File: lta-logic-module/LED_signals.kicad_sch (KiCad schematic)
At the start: 12 parts

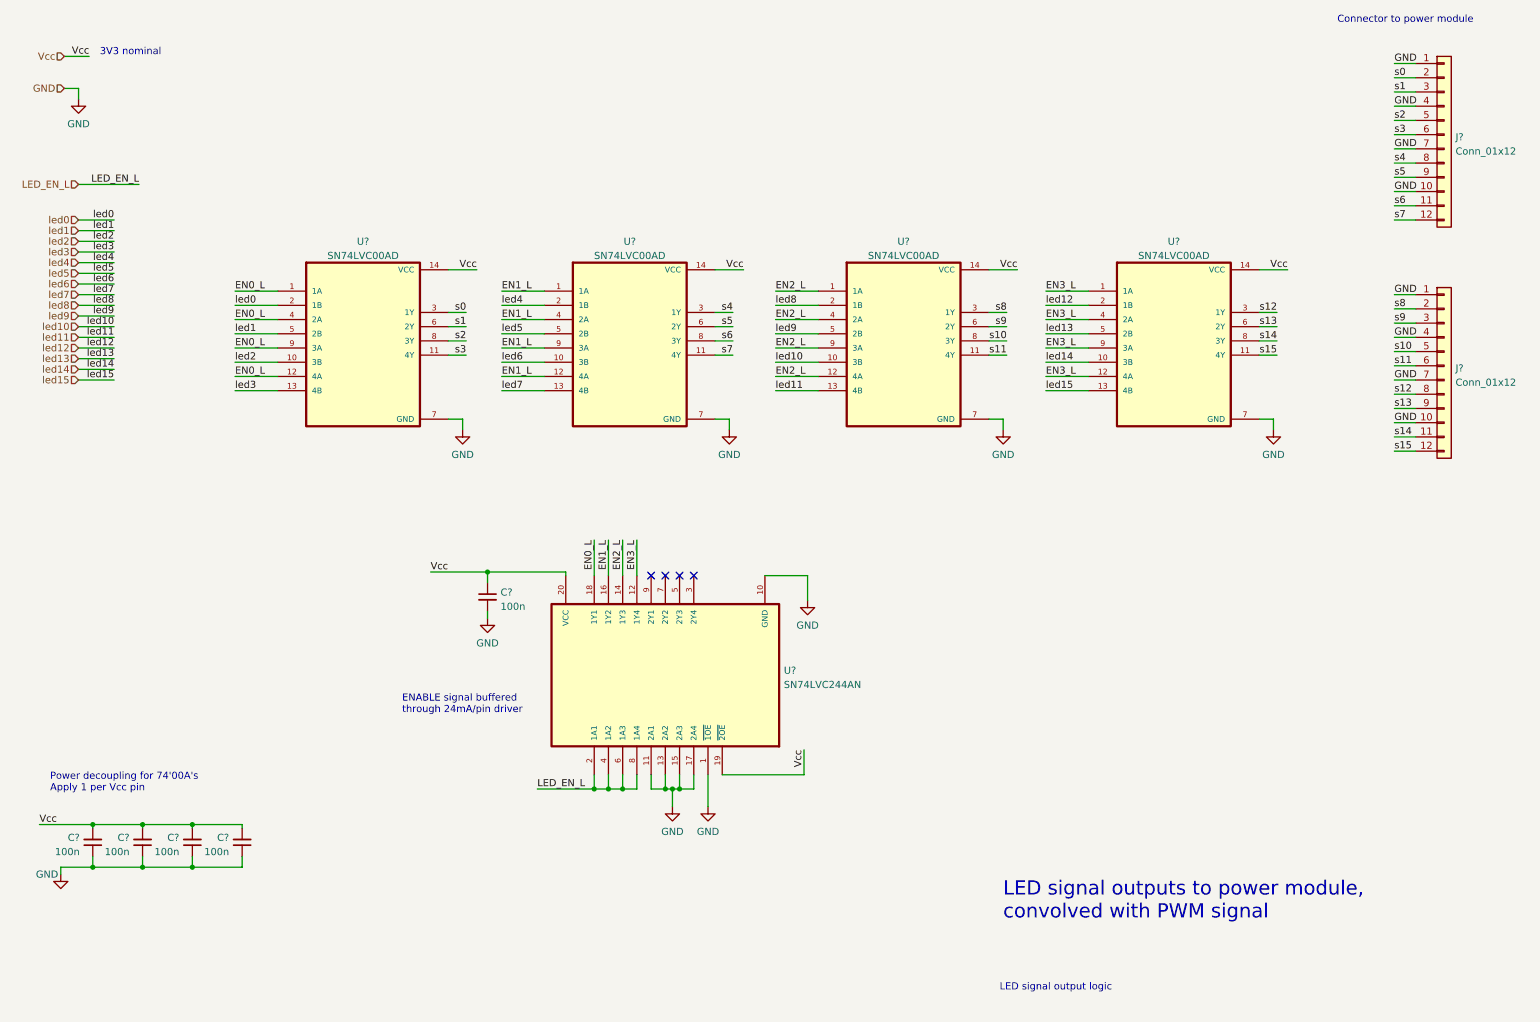
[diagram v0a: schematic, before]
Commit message: Fix ERC violations.
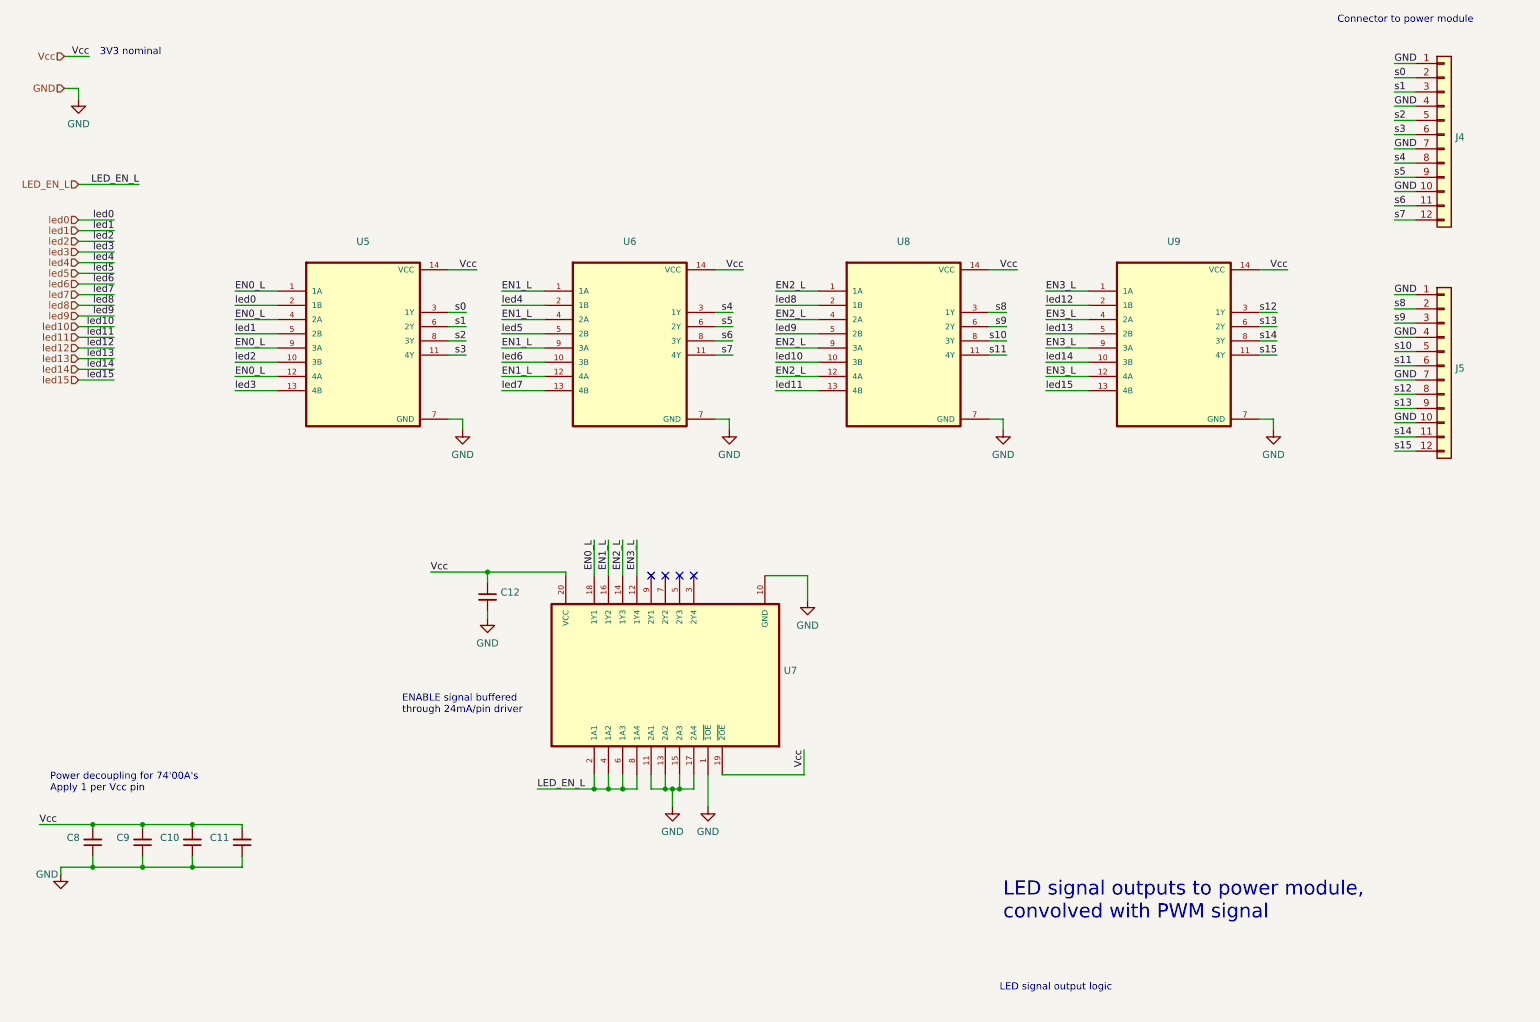
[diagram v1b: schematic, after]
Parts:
- C10, C11, C12, C8, C9: renamed from C?; value 100n -> (none)
- J4, J5: renamed from J?; value Conn_01x12 -> (none)
- U5, U6, U8, U9: renamed from U?; value SN74LVC00AD -> (none); footprint Aaron_TI_Parts:TI_SOIC_D_R-PDSO-G14 -> (none)
- U7: renamed from U?; value SN74LVC244AN -> (none); footprint Aaron_TI_Parts:TI_N_R-PDIP-T20 -> (none)

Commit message: Add TODOs, update some footprints.
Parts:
- C10, C11, C12, C8, C9: value (none) -> 100n; footprint (none) -> Capacitor_SMD:C_0603_1608Metric; Comment (none) -> 100nF 5% 6.3V 0603 X7R ceramic; 20mOhm < ESR < 10 Ohm; MANUFACTURER (none) -> KYOCERA; MPN (none) -> 06036C104JAT2A
- J4, J5: value (none) -> Conn_01x12; footprint (none) -> Connector_PinHeader_2.54mm:PinHeader_1x12_P2.54mm_Vertical; Comment (none) -> TODO REPLACE FOOTPRINT; MPN (none) -> XXX TODO FIND
- U5, U6, U8, U9: value (none) -> SN74LVC00AD; footprint (none) -> Aaron_TI_Parts:TI_SOIC_D_R-PDSO-G14; MANUFACTURER (none) -> Texas Instruments; MPN (none) -> SN74LVC00AD
- U7: value (none) -> SN74LVC244AN; footprint (none) -> Aaron_TI_Parts:TI_N_R-PDIP-T20; MANUFACTURER (none) -> Texas Instruments; MPN (none) -> SN74LVC244AN

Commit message: Initial PCB setup
* Configure Elecrow DRC checks for lta-logic-module.
* Switch SN74LVC244A from 'N' PDIP to 'DWR' SOIC footprint.
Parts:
- removed U7: SN74LVC244AN, Aaron_TI_Parts:TI_N_R-PDIP-T20, symbol Aaron-TI-Buffers:SN74LVC244AN
- added U8: (no value), Aaron_TI_Parts:TI_SOIC_DW0020A, symbol Aaron-TI-Buffers:SN74LVC244ADW
- renumbered C8 to C12, C9 to C13, C10 to C14, C11 to C15, C12 to C16, J4 to J3, J5 to J4, U9 to U10, U5 to U6, U6 to U7, U8 to U9
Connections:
- net EN0_L: now also U8.18 (1Y1)
- net EN1_L: now also U8.16 (1Y2)
- net EN2_L: now also U8.14 (1Y3)
- net EN3_L: now also U8.12 (1Y4)
- net GND: now also U8.1 (~{1OE}), U8.10 (GND), U8.11 (2A1), U8.13 (2A2), U8.15 (2A3), U8.17 (2A4)
- net LED_EN_L: now also U8.2 (1A1), U8.4 (1A2), U8.6 (1A3), U8.8 (1A4)
- net Vcc: now also U8.19 (~{2OE}), U8.20 (VCC)
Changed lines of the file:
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@@
   (symbol (lib_id "Device:C_Small") (at 28.575 163.83 0) (mirror x) (unit 1)
     (in_bom yes) (on_board yes) (fields_autoplaced)
-    (property "Reference" "C8" (id 0) (at 26.2509 162.9889 0)
+    (property "Reference" "C12" (id 0) (at 26.2509 162.9889 0)
       (effects (font (size 1.27 1.27)) (justify right))
     )
@@
   (symbol (lib_id "power:GND") (at 191.135 90.17 0) (unit 1)
     (in_bom yes) (on_board yes) (fields_autoplaced)
-    (property "Reference" "#PWR039" (id 0) (at 191.135 96.52 0)
+    (property "Reference" "#PWR040" (id 0) (at 191.135 96.52 0)
       (effects (font (size 1.27 1.27)) hide)
     )
@@
   (symbol (lib_id "Aaron-TI-74xx:SN74LVC00AD") (at 79.375 78.105 0) (unit 1)
     (in_bom yes) (on_board yes) (fields_autoplaced)
-    (property "Reference" "U5" (id 0) (at 76.835 56.549 0))
+    (property "Reference" "U6" (id 0) (at 76.835 56.549 0))
     (property "Value" "SN74LVC00AD" (id 1) (at 76.835 59.0859 0))
     (property "Footprint" "Aaron_TI_Parts:TI_SOIC_D_R-PDSO-G14" (id 2) (at 74.295 80.645 0)
@@
   (symbol (lib_id "Device:C_Small") (at 55.245 163.83 0) (mirror x) (unit 1)
     (in_bom yes) (on_board yes) (fields_autoplaced)
-    (property "Reference" "C11" (id 0) (at 52.9209 162.9889 0)
+    (property "Reference" "C15" (id 0) (at 52.9209 162.9889 0)
       (effects (font (size 1.27 1.27)) (justify right))
     )
@@
   (symbol (lib_id "Connector_Generic:Conn_01x12") (at 269.875 37.465 0) (unit 1)
     (in_bom yes) (on_board yes) (fields_autoplaced)
-    (property "Reference" "J4" (id 0) (at 271.907 37.9003 0)
+    (property "Reference" "J3" (id 0) (at 271.907 37.9003 0)
       (effects (font (size 1.27 1.27)) (justify left))
     )
@@
   (symbol (lib_id "Aaron-TI-74xx:SN74LVC00AD") (at 224.155 78.105 0) (unit 1)
     (in_bom yes) (on_board yes) (fields_autoplaced)
-    (property "Reference" "U9" (id 0) (at 221.615 56.549 0))
+    (property "Reference" "U10" (id 0) (at 221.615 56.549 0))
     (property "Value" "SN74LVC00AD" (id 1) (at 221.615 59.0859 0))
     (property "Footprint" "Aaron_TI_Parts:TI_SOIC_D_R-PDSO-G14" (id 2) (at 219.075 80.645 0)
@@
   (symbol (lib_id "power:GND") (at 22.86 169.545 0) (unit 1)
     (in_bom yes) (on_board yes)
-    (property "Reference" "#PWR031" (id 0) (at 22.86 175.895 0)
+    (property "Reference" "#PWR032" (id 0) (at 22.86 175.895 0)
       (effects (font (size 1.27 1.27)) hide)
     )
@@
   (symbol (lib_id "power:GND") (at 239.395 90.17 0) (unit 1)
     (in_bom yes) (on_board yes) (fields_autoplaced)
-    (property "Reference" "#PWR040" (id 0) (at 239.395 96.52 0)
+    (property "Reference" "#PWR041" (id 0) (at 239.395 96.52 0)
       (effects (font (size 1.27 1.27)) hide)
     )
@@
   (symbol (lib_id "Device:C_Small") (at 99.06 120.015 0) (unit 1)
     (in_bom yes) (on_board yes)
-    (property "Reference" "C12" (id 0) (at 101.3841 119.1866 0)
+    (property "Reference" "C16" (id 0) (at 101.3841 119.1866 0)
       (effects (font (size 1.27 1.27)) (justify left))
     )
@@
   (symbol (lib_id "Device:C_Small") (at 37.465 163.83 0) (mirror x) (unit 1)
     (in_bom yes) (on_board yes) (fields_autoplaced)
-    (property "Reference" "C9" (id 0) (at 35.1409 162.9889 0)
+    (property "Reference" "C13" (id 0) (at 35.1409 162.9889 0)
       (effects (font (size 1.27 1.27)) (justify right))
     )
@@
   (symbol (lib_id "Aaron-TI-74xx:SN74LVC00AD") (at 127 78.105 0) (unit 1)
     (in_bom yes) (on_board yes) (fields_autoplaced)
-    (property "Reference" "U6" (id 0) (at 124.46 56.549 0))
+    (property "Reference" "U7" (id 0) (at 124.46 56.549 0))
     (property "Value" "SN74LVC00AD" (id 1) (at 124.46 59.0859 0))
     (property "Footprint" "Aaron_TI_Parts:TI_SOIC_D_R-PDSO-G14" (id 2) (at 121.92 80.645 0)
@@
     (pin "9")
   )
-  (symbol (lib_id "Aaron-TI-Buffers:SN74LVC244AN") (at 130.81 133.985 90) (unit 1)
-    (in_bom yes) (on_board yes) (fields_autoplaced)
-    (property "Reference" "U7" (id 0) (at 151.9682 133.1503 90)
-      (effects (font (size 1.27 1.27)) (justify right))
-    )
-    (property "Value" "SN74LVC244AN" (id 1) (at 151.9682 135.6872 90)
-      (effects (font (size 1.27 1.27)) (justify right))
-    )
-    (property "Footprint" "Aaron_TI_Parts:TI_N_R-PDIP-T20" (id 2) (at 130.81 133.985 0)
+  (symbol (lib_id "Aaron-TI-Buffers:SN74LVC244ADW") (at 130.81 133.985 90) (unit 1)
+    (in_bom yes) (on_board yes) (fields_autoplaced)
+    (property "Reference" "U8" (id 0) (at 151.9682 130.6134 90)
+      (effects (font (size 1.27 1.27)) (justify right))
+    )
+    (property "Value" "" (id 1) (at 151.9682 133.1503 90)
+      (effects (font (size 1.27 1.27)) (justify right))
+    )
+    (property "Footprint" "Aaron_TI_Parts:TI_SOIC_DW0020A" (id 2) (at 130.81 133.985 0)
       (effects (font (size 1.27 1.27)) (justify left bottom) hide)
     )
@@
       (effects (font (size 1.27 1.27)) (justify left bottom) hide)
     )
-    (property "MANUFACTURER" "Texas Instruments" (id 4) (at 130.81 133.985 0)
-      (effects (font (size 1.27 1.27)) hide)
-    )
-    (property "MPN" "SN74LVC244AN" (id 5) (at 130.81 133.985 0)
-      (effects (font (size 1.27 1.27)) hide)
+    (property "MANUFACTURER" "Texas Instruments" (id 4) (at 151.9682 135.6872 90)
+      (effects (font (size 1.27 1.27)) (justify right) hide)
+    )
+    (property "MPN" "SN74LVC244ADWR" (id 5) (at 151.9682 138.2241 90)
+      (effects (font (size 1.27 1.27)) (justify right) hide)
     )
     (pin "1")
@@
   (symbol (lib_id "power:GND") (at 156.21 120.65 0) (unit 1)
     (in_bom yes) (on_board yes) (fields_autoplaced)
-    (property "Reference" "#PWR038" (id 0) (at 156.21 127 0)
+    (property "Reference" "#PWR039" (id 0) (at 156.21 127 0)
       (effects (font (size 1.27 1.27)) hide)
     )
@@
   (symbol (lib_id "power:GND") (at 99.06 123.825 0) (unit 1)
     (in_bom yes) (on_board yes) (fields_autoplaced)
-    (property "Reference" "#PWR034" (id 0) (at 99.06 130.175 0)
+    (property "Reference" "#PWR035" (id 0) (at 99.06 130.175 0)
       (effects (font (size 1.27 1.27)) hide)
     )
@@
   (symbol (lib_id "power:GND") (at 142.24 90.17 0) (unit 1)
     (in_bom yes) (on_board yes) (fields_autoplaced)
-    (property "Reference" "#PWR037" (id 0) (at 142.24 96.52 0)
+    (property "Reference" "#PWR038" (id 0) (at 142.24 96.52 0)
       (effects (font (size 1.27 1.27)) hide)
     )
@@
   (symbol (lib_id "Device:C_Small") (at 46.355 163.83 0) (mirror x) (unit 1)
     (in_bom yes) (on_board yes) (fields_autoplaced)
-    (property "Reference" "C10" (id 0) (at 44.0309 162.9889 0)
+    (property "Reference" "C14" (id 0) (at 44.0309 162.9889 0)
       (effects (font (size 1.27 1.27)) (justify right))
     )
@@
   (symbol (lib_id "power:GND") (at 132.08 157.48 0) (unit 1)
     (in_bom yes) (on_board yes) (fields_autoplaced)
-    (property "Reference" "#PWR035" (id 0) (at 132.08 163.83 0)
+    (property "Reference" "#PWR036" (id 0) (at 132.08 163.83 0)
       (effects (font (size 1.27 1.27)) hide)
     )
@@
   (symbol (lib_id "power:GND") (at 138.43 157.48 0) (unit 1)
     (in_bom yes) (on_board yes) (fields_autoplaced)
-    (property "Reference" "#PWR036" (id 0) (at 138.43 163.83 0)
+    (property "Reference" "#PWR037" (id 0) (at 138.43 163.83 0)
       (effects (font (size 1.27 1.27)) hide)
     )
@@
   (symbol (lib_id "Aaron-TI-74xx:SN74LVC00AD") (at 175.895 78.105 0) (unit 1)
     (in_bom yes) (on_board yes) (fields_autoplaced)
-    (property "Reference" "U8" (id 0) (at 173.355 56.549 0))
+    (property "Reference" "U9" (id 0) (at 173.355 56.549 0))
     (property "Value" "SN74LVC00AD" (id 1) (at 173.355 59.0859 0))
     (property "Footprint" "Aaron_TI_Parts:TI_SOIC_D_R-PDSO-G14" (id 2) (at 170.815 80.645 0)
@@
   (symbol (lib_id "power:GND") (at 26.035 31.115 0) (unit 1)
     (in_bom yes) (on_board yes) (fields_autoplaced)
-    (property "Reference" "#PWR032" (id 0) (at 26.035 37.465 0)
+    (property "Reference" "#PWR033" (id 0) (at 26.035 37.465 0)
       (effects (font (size 1.27 1.27)) hide)
     )
@@
   (symbol (lib_id "power:GND") (at 94.615 90.17 0) (unit 1)
     (in_bom yes) (on_board yes) (fields_autoplaced)
-    (property "Reference" "#PWR033" (id 0) (at 94.615 96.52 0)
+    (property "Reference" "#PWR034" (id 0) (at 94.615 96.52 0)
       (effects (font (size 1.27 1.27)) hide)
     )
@@
   (symbol (lib_id "Connector_Generic:Conn_01x12") (at 269.875 78.74 0) (unit 1)
     (in_bom yes) (on_board yes) (fields_autoplaced)
-    (property "Reference" "J5" (id 0) (at 271.907 79.1753 0)
-      (effects (font (size 1.27 1.27)) (justify left))
-    )
+    (property "Reference" "J4" (id 0) (at 271.907 79.1753 0)
+      (effects (font (size 1.27 1.27)) (justify left))
+    )
